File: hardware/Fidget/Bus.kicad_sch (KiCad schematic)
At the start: 5 parts

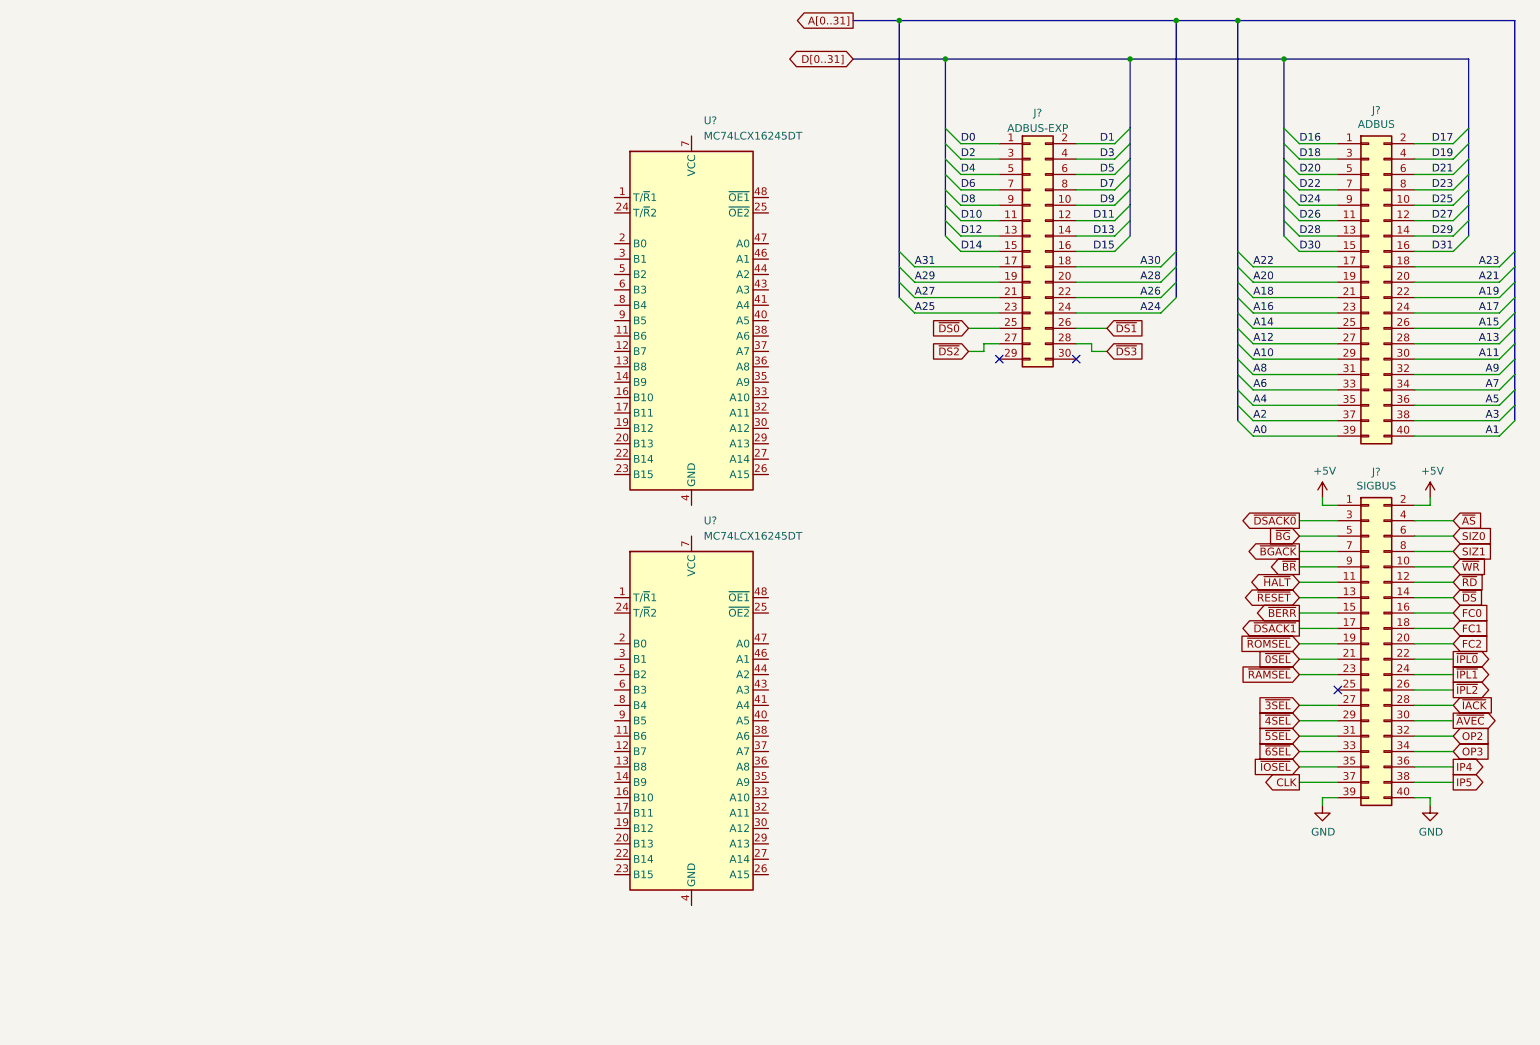
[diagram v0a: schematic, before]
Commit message: Added level shifting and some I/O assignments
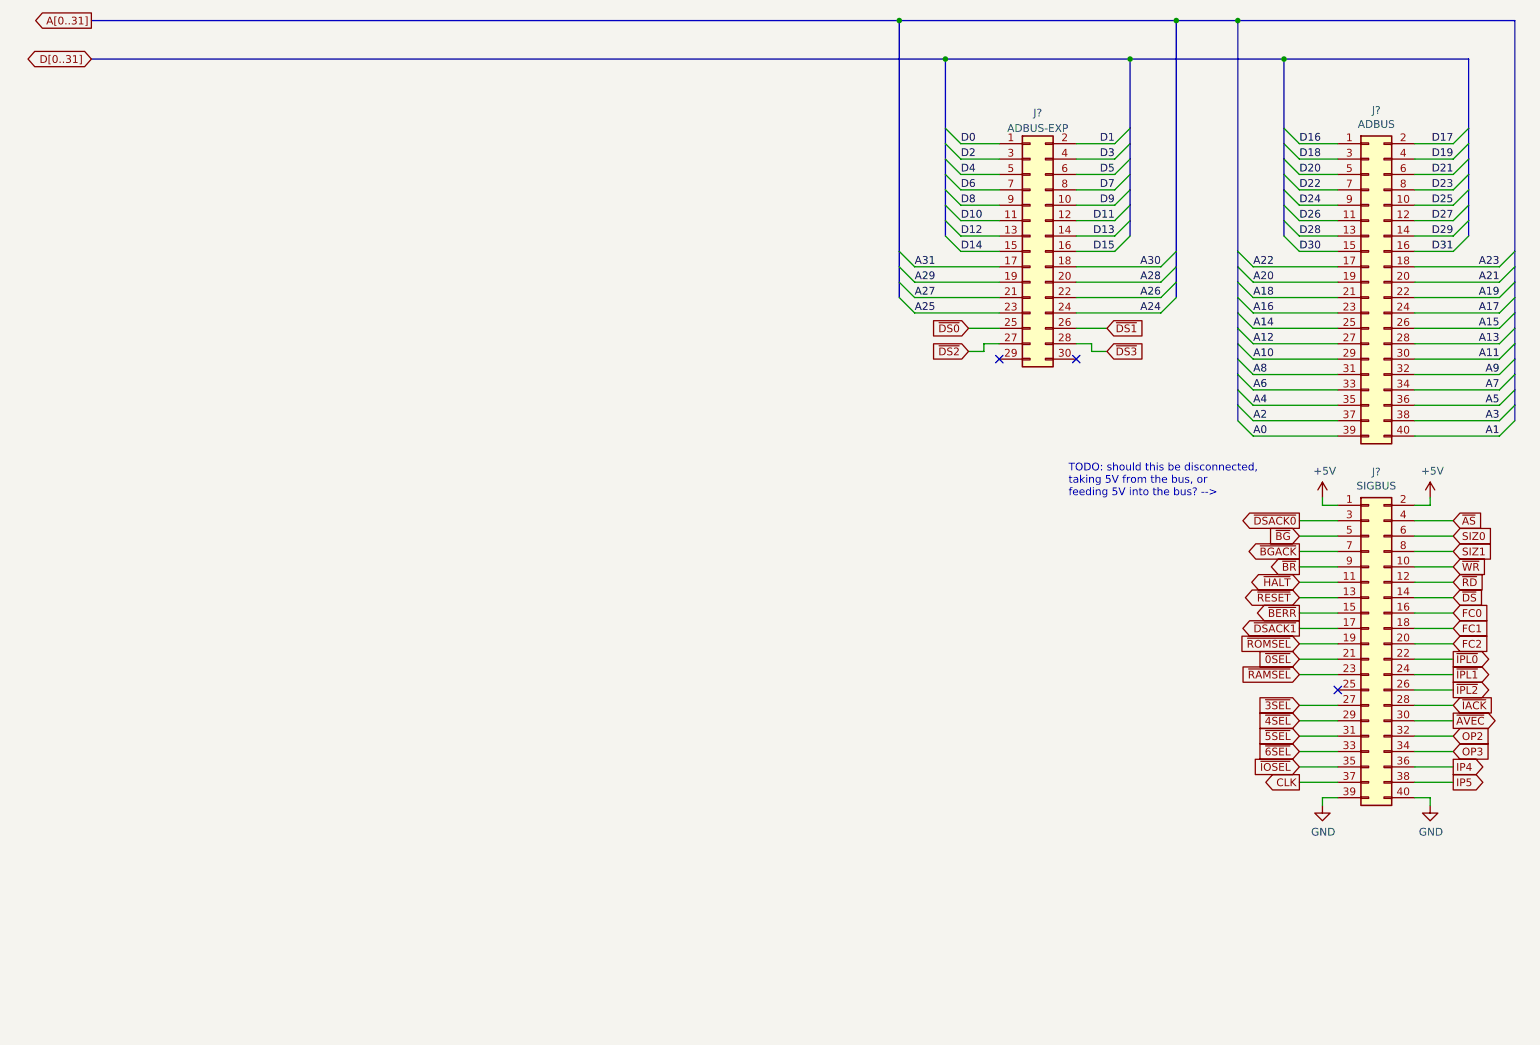
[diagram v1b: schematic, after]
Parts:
- removed U? (x2): MC74LCX16245DT, Package_SO:TSSOP-48_6.1x12.5mm_P0.5mm, symbol 74xx:MC74LCX16245DT
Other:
- note added: "TODO: should this be disconnected, taking 5V from the bus, or feeding 5V into the bus? -->"
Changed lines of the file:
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@@
-    (stroke (width 0) (type default) (color 0 0 0 0))
-  )
-  (bus (pts (xy 175.26 30.48) (xy 160.02 30.48))
     (stroke (width 0) (type default) (color 0 0 0 0))
   )
@@
     (stroke (width 0) (type default) (color 0 0 0 0))
   )
+  (bus (pts (xy 34.29 30.48) (xy 175.26 30.48))
+    (stroke (width 0) (type default) (color 0 0 0 0))
+  )
   (wire (pts (xy 210.82 64.77) (xy 196.85 64.77))
     (stroke (width 0) (type default) (color 0 0 0 0))
@@
     (stroke (width 0) (type default) (color 0 0 0 0))
   )
+  (bus (pts (xy 34.29 24.13) (xy 167.64 24.13))
+    (stroke (width 0) (type default) (color 0 0 0 0))
+  )
   (wire (pts (xy 252.73 54.61) (xy 259.08 54.61))
     (stroke (width 0) (type default) (color 0 0 0 0))
@@
     (stroke (width 0) (type default) (color 0 0 0 0))
   )
-  (bus (pts (xy 167.64 24.13) (xy 160.02 24.13))
-    (stroke (width 0) (type default) (color 0 0 0 0))
-  )
   (bus (pts (xy 269.24 74.93) (xy 269.24 77.47))
     (stroke (width 0) (type default) (color 0 0 0 0))
@@
     (stroke (width 0) (type default) (color 0 0 0 0))
   )
+  (text "TODO: should this be disconnected,\ntaking 5V from the bus, or\nfeeding 5V into the bus? -->"
+    (at 195.58 102.87 0)
+    (effects (font (size 1.27 1.27)) (justify left bottom))
+  )
   (label "D9" (at 203.2 54.61 180)
     (effects (font (size 1.27 1.27)) (justify right bottom))
@@
     )
   )
-  (global_label "A[0..31]" (shape output) (at 160.02 24.13 180) (fields_autoplaced)
-    (effects (font (size 1.27 1.27)) (justify right))
-    (property "Intersheet References" "${INTERSHEET_REFS}" (id 0) (at 129.54 -2.54 0)
+  (global_label "A[0..31]" (shape output) (at 34.29 24.13 180) (fields_autoplaced)
+    (effects (font (size 1.27 1.27)) (justify right))
+    (property "Intersheet References" "${INTERSHEET_REFS}" (id 0) (at 3.81 -2.54 0)
       (effects (font (size 1.27 1.27)) hide)
     )
@@
     )
   )
-  (global_label "D[0..31]" (shape bidirectional) (at 160.02 30.48 180) (fields_autoplaced)
-    (effects (font (size 1.27 1.27)) (justify right))
-    (property "Intersheet References" "${INTERSHEET_REFS}" (id 0) (at 129.54 -2.54 0)
+  (global_label "D[0..31]" (shape bidirectional) (at 34.29 30.48 180) (fields_autoplaced)
+    (effects (font (size 1.27 1.27)) (justify right))
+    (property "Intersheet References" "${INTERSHEET_REFS}" (id 0) (at 3.81 -2.54 0)
       (effects (font (size 1.27 1.27)) hide)
     )
@@
     (pin "9")
   )
-  (symbol (lib_id "74xx:MC74LCX16245DT") (at 133.35 139.7 0) (unit 1)
-    (in_bom yes) (on_board yes) (fields_autoplaced)
-    (property "Reference" "U?" (id 0) (at 135.3694 106.68 0)
-      (effects (font (size 1.27 1.27)) (justify left))
-    )
-    (property "Value" "MC74LCX16245DT" (id 1) (at 135.3694 109.22 0)
-      (effects (font (size 1.27 1.27)) (justify left))
-    )
-    (property "Footprint" "Package_SO:TSSOP-48_6.1x12.5mm_P0.5mm" (id 2) (at 133.35 140.97 0)
-      (effects (font (size 1.27 1.27) italic) hide)
-    )
-    (property "Datasheet" "https://www.onsemi.com/pdf/datasheet/mc74lcx16245-d.pdf" (id 3) (at 133.35 143.51 0)
-      (effects (font (size 1.27 1.27)) hide)
-    )
-    (pin "1")
-    (pin "10")
-    (pin "11")
-    (pin "12")
-    (pin "13")
-    (pin "14")
-    (pin "15")
-    (pin "16")
-    (pin "17")
-    (pin "18")
-    (pin "19")
-    (pin "2")
-    (pin "20")
-    (pin "21")
-    (pin "22")
-    (pin "23")
-    (pin "24")
-    (pin "25")
-    (pin "26")
-    (pin "27")
-    (pin "28")
-    (pin "29")
-    (pin "3")
-    (pin "30")
-    (pin "31")
-    (pin "32")
-    (pin "33")
-    (pin "34")
-    (pin "35")
-    (pin "36")
-    (pin "37")
-    (pin "38")
-    (pin "39")
-    (pin "4")
-    (pin "40")
-    (pin "41")
-    (pin "42")
-    (pin "43")
-    (pin "44")
-    (pin "45")
-    (pin "46")
-    (pin "47")
-    (pin "48")
-    (pin "5")
-    (pin "6")
-    (pin "7")
-    (pin "8")
-    (pin "9")
-  )
   (symbol (lib_id "Connector_Generic:Conn_02x15_Odd_Even") (at 189.23 62.23 0) (unit 1)
     (in_bom yes) (on_board yes)
@@
     (pin "9")
   )
-  (symbol (lib_id "74xx:MC74LCX16245DT") (at 133.35 73.66 0) (unit 1)
-    (in_bom yes) (on_board yes) (fields_autoplaced)
-    (property "Reference" "U?" (id 0) (at 135.3694 40.64 0)
-      (effects (font (size 1.27 1.27)) (justify left))
-    )
-    (property "Value" "MC74LCX16245DT" (id 1) (at 135.3694 43.18 0)
-      (effects (font (size 1.27 1.27)) (justify left))
-    )
-    (property "Footprint" "Package_SO:TSSOP-48_6.1x12.5mm_P0.5mm" (id 2) (at 133.35 74.93 0)
-      (effects (font (size 1.27 1.27) italic) hide)
-    )
-    (property "Datasheet" "https://www.onsemi.com/pdf/datasheet/mc74lcx16245-d.pdf" (id 3) (at 133.35 77.47 0)
-      (effects (font (size 1.27 1.27)) hide)
-    )
-    (pin "1")
-    (pin "10")
-    (pin "11")
-    (pin "12")
-    (pin "13")
-    (pin "14")
-    (pin "15")
-    (pin "16")
-    (pin "17")
-    (pin "18")
-    (pin "19")
-    (pin "2")
-    (pin "20")
-    (pin "21")
-    (pin "22")
-    (pin "23")
-    (pin "24")
-    (pin "25")
-    (pin "26")
-    (pin "27")
-    (pin "28")
-    (pin "29")
-    (pin "3")
-    (pin "30")
-    (pin "31")
-    (pin "32")
-    (pin "33")
-    (pin "34")
-    (pin "35")
-    (pin "36")
-    (pin "37")
-    (pin "38")
-    (pin "39")
-    (pin "4")
-    (pin "40")
-    (pin "41")
-    (pin "42")
-    (pin "43")
-    (pin "44")
-    (pin "45")
-    (pin "46")
-    (pin "47")
-    (pin "48")
-    (pin "5")
-    (pin "6")
-    (pin "7")
-    (pin "8")
-    (pin "9")
-  )
   (symbol (lib_id "power:+5V") (at 237.49 102.87 0) (unit 1)
     (in_bom yes) (on_board yes)
-    (property "Reference" "#PWR?" (id 0) (at 237.49 106.68 0)
+    (property "Reference" "#PWR0143" (id 0) (at 237.49 106.68 0)
       (effects (font (size 1.27 1.27)) hide)
     )
@@
   (symbol (lib_id "power:GND") (at 255.27 153.67 0) (unit 1)
     (in_bom yes) (on_board yes)
-    (property "Reference" "#PWR?" (id 0) (at 255.27 160.02 0)
+    (property "Reference" "#PWR0141" (id 0) (at 255.27 160.02 0)
       (effects (font (size 1.27 1.27)) hide)
     )
@@
   (symbol (lib_id "power:+5V") (at 255.27 102.87 0) (unit 1)
     (in_bom yes) (on_board yes)
-    (property "Reference" "#PWR?" (id 0) (at 255.27 106.68 0)
+    (property "Reference" "#PWR0144" (id 0) (at 255.27 106.68 0)
       (effects (font (size 1.27 1.27)) hide)
     )
@@
   (symbol (lib_id "power:GND") (at 237.49 153.67 0) (unit 1)
     (in_bom yes) (on_board yes)
-    (property "Reference" "#PWR?" (id 0) (at 237.49 160.02 0)
-      (effects (font (size 1.27 1.27)) hide)
-    )
+    (property "Reference" "#PWR0142" (id 0) (at 237.49 160.02 0)
+      (effects (font (size 1.27 1.27)) hide)
+    )

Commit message: Added address latches
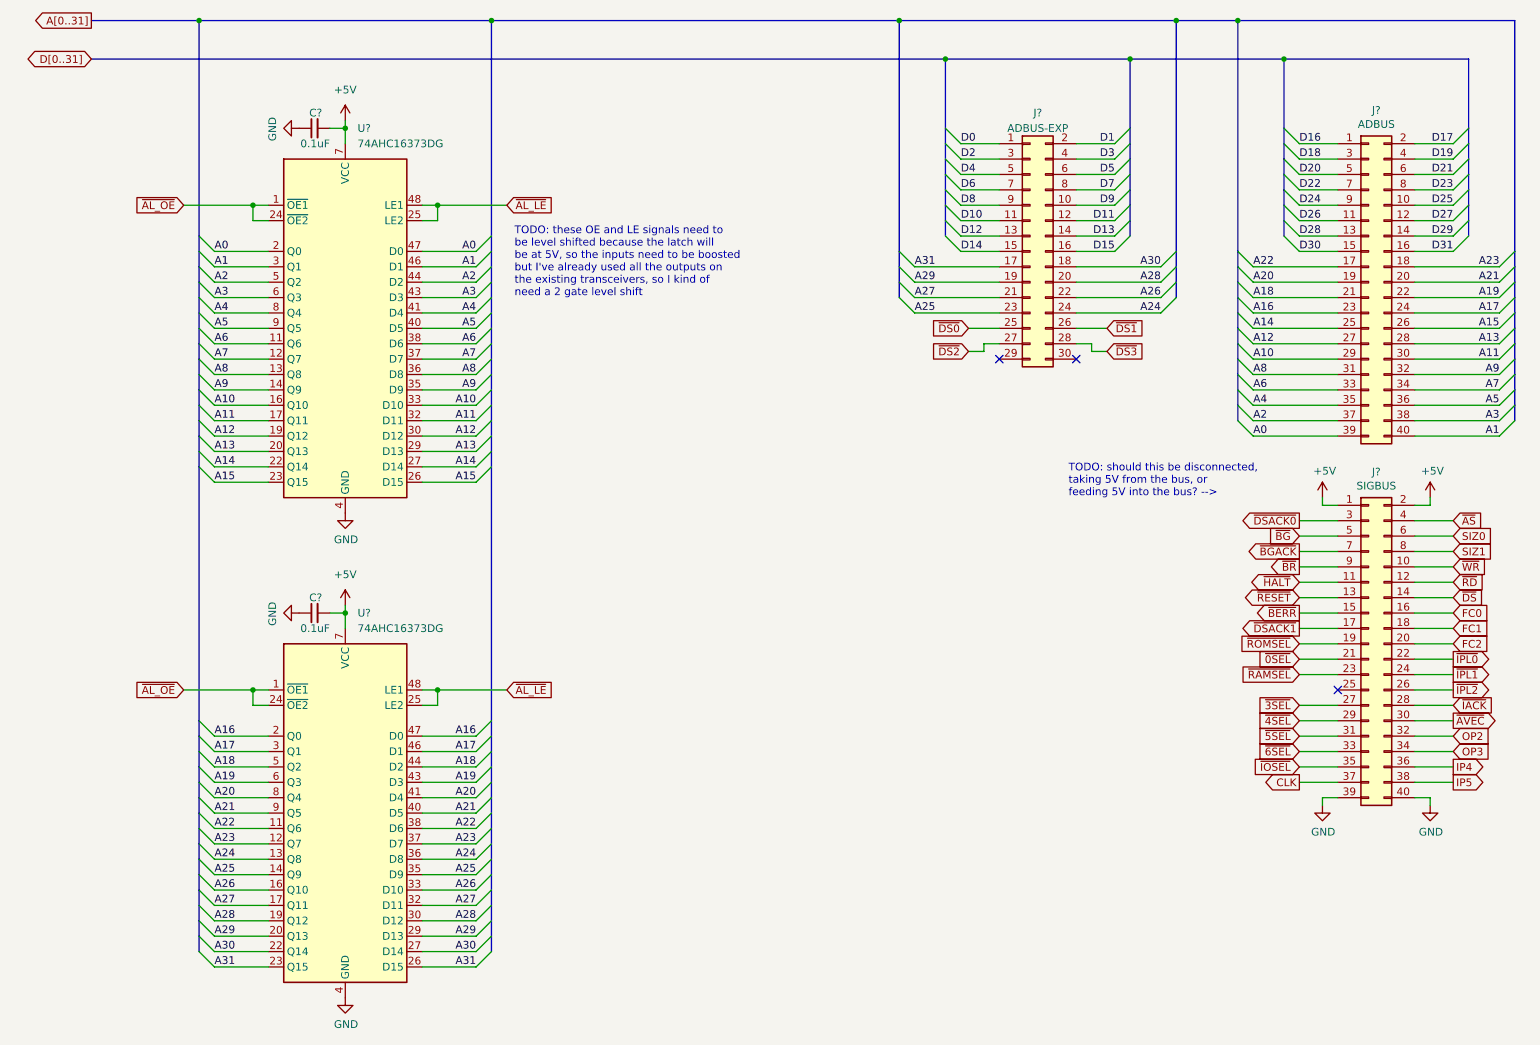
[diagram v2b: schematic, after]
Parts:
- added C? (x2): 0.1uF, symbol Device:C_Small
- added U? (x2): 74AHC16373DG, Package_SO:TSSOP-48_6.1x12.5mm_P0.5mm, symbol Fidget:74AHC16373DG
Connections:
- net +5V: now also C?.2, C?.2, U?.18 (VCC), U?.18 (VCC), U?.31 (VCC), U?.31 (VCC), U?.42 (VCC), U?.42 (VCC), U?.7 (VCC), U?.7 (VCC)
- net A0: now also U?.2 (Q0), U?.47 (D0)
- net A1: now also U?.3 (Q1), U?.46 (D1)
- net A10: now also U?.16 (Q10), U?.33 (D10)
- net A11: now also U?.17 (Q11), U?.32 (D11)
- net A12: now also U?.19 (Q12), U?.30 (D12)
- net A13: now also U?.20 (Q13), U?.29 (D13)
- net A14: now also U?.22 (Q14), U?.27 (D14)
- net A15: now also U?.23 (Q15), U?.26 (D15)
- net A16: now also U?.2 (Q0), U?.47 (D0)
- net A17: now also U?.3 (Q1), U?.46 (D1)
- net A18: now also U?.44 (D2), U?.5 (Q2)
- net A19: now also U?.43 (D3), U?.6 (Q3)
- net A2: now also U?.44 (D2), U?.5 (Q2)
- net A20: now also U?.41 (D4), U?.8 (Q4)
- net A21: now also U?.40 (D5), U?.9 (Q5)
- net A22: now also U?.11 (Q6), U?.38 (D6)
- net A23: now also U?.12 (Q7), U?.37 (D7)
- net A24: now also U?.13 (Q8), U?.36 (D8)
- net A25: now also U?.14 (Q9), U?.35 (D9)
- net A26: now also U?.16 (Q10), U?.33 (D10)
- net A27: now also U?.17 (Q11), U?.32 (D11)
- net A28: now also U?.19 (Q12), U?.30 (D12)
- net A29: now also U?.20 (Q13), U?.29 (D13)
- net A3: now also U?.43 (D3), U?.6 (Q3)
- net A30: now also U?.22 (Q14), U?.27 (D14)
- net A31: now also U?.23 (Q15), U?.26 (D15)
- net A4: now also U?.41 (D4), U?.8 (Q4)
- net A5: now also U?.40 (D5), U?.9 (Q5)
- net A6: now also U?.11 (Q6), U?.38 (D6)
- net A7: now also U?.12 (Q7), U?.37 (D7)
- net A8: now also U?.13 (Q8), U?.36 (D8)
- net A9: now also U?.14 (Q9), U?.35 (D9)
- net GND: now also C?.1, C?.1, U?.10 (GND), U?.10 (GND), U?.15 (GND), U?.15 (GND), U?.21 (GND), U?.21 (GND), U?.28 (GND), U?.28 (GND), U?.34 (GND), U?.34 (GND), U?.39 (GND), U?.39 (GND), U?.4 (GND), U?.4 (GND), U?.45 (GND), U?.45 (GND)
- new net ~{AL_LE}: U?.25 (LE2), U?.25 (LE2), U?.48 (LE1), U?.48 (LE1)
- new net ~{AL_OE}: U?.1 (~{OE1}), U?.1 (~{OE1}), U?.24 (~{OE2}), U?.24 (~{OE2})
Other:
- note added: "TODO: these OE and LE signals need to be level shifted because the latch will be at 5V, so the inputs need to be boosted but I've already used all the outputs on the existing transceivers, so I kind of need a 2 gate level shift"
